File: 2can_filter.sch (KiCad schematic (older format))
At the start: 17 parts

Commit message: finish scheme & change libs path
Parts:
- removed C? (x2): 10pF, symbol C
- removed J?: USB_OTG, symbol USB_OTG
- removed R? (x2): 60, symbol R
- removed R?: 10k, symbol R
- removed U?: STM32F105RBTx, LQFP64, symbol STM32F105RBTx
- removed U?: TJA1040T, Housings_SOIC:SOIC-8_3.9x4.9mm_Pitch1.27mm, symbol TJA1040T
- added C11, C12: 10pF, symbol C
- added J3: USB mini-B SMD, 54819-0572:MOLEXMINIBTYPEB_1, symbol 54819-0572
- added R2: 10k, symbol R
- added R3, R4: 60, symbol R
- added R? (x2): 22, symbol R
- added U5: STM32F105RBTx, Housings_QFP:LQFP-64_10x10mm_Pitch0.5mm, symbol STM32F105RBTx
- added U6: TJA1040T, Housings_SOIC:SOIC-8_3.9x4.9mm_Pitch1.27mm, symbol TJA1040T
- gave numbers to parts that had none: 9
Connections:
- wire segments 75 -> 77
- no-connect marks 43 -> 42
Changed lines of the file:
@@
 LIBS:LM2596SX-5.0_NOPB
 LIBS:lm2575s-5
+LIBS:74HC4050D
+LIBS:54819-0572
 LIBS:instrument_cluster-cache
 EELAYER 25 0
@@
 $EndDescr
 $Comp
-L STM32F105RBTx U?
-U 1 1 5A047502
+L STM32F105RBTx U5
+U 1 1 5A09EB17
 P 4900 2900
-F 0 "U?" H 2200 4825 50  0000 L BNN
+F 0 "U5" H 2200 4825 50  0000 L BNN
 F 1 "STM32F105RBTx" H 7600 4825 50  0000 R BNN
-F 2 "LQFP64" H 7600 4775 50  0001 R TNN
+F 2 "Housings_QFP:LQFP-64_10x10mm_Pitch0.5mm" H 7600 4775 50  0001 R TNN
 F 3 "" H 4900 2900 50  0001 C CNN
 	1    4900 2900
@@
 $EndComp
 $Comp
-L TJA1040T U?
-U 1 1 5A047692
+L TJA1040T U6
+U 1 1 5A09EB18
 P 9800 4150
-F 0 "U?" H 9400 4500 50  0000 L CNN
+F 0 "U6" H 9400 4500 50  0000 L CNN
 F 1 "TJA1040T" H 9850 4500 50  0000 L CNN
 F 2 "Housings_SOIC:SOIC-8_3.9x4.9mm_Pitch1.27mm" H 9800 3650 50  0001 C CIN
@@
 CAN2_L
 $Comp
-L TJA1040T U?
+L TJA1040T U7
 U 1 1 5A0478A4
 P 9800 5550
-F 0 "U?" H 9400 5900 50  0000 L CNN
+F 0 "U7" H 9400 5900 50  0000 L CNN
 F 1 "TJA1040T" H 9850 5900 50  0000 L CNN
 F 2 "Housings_SOIC:SOIC-8_3.9x4.9mm_Pitch1.27mm" H 9800 5050 50  0001 C CIN
@@
 	1500 6500 1950 6500
 $Comp
-L C C?
-U 1 1 5A047AB3
+L C C11
+U 1 1 5A09EB1A
 P 10900 4450
-F 0 "C?" H 10925 4550 50  0000 L CNN
+F 0 "C11" H 10925 4550 50  0000 L CNN
 F 1 "10pF" H 10925 4350 50  0000 L CNN
 F 2 "" H 10938 4300 50  0001 C CNN
@@
 $EndComp
 $Comp
-L R R?
-U 1 1 5A047B18
+L R R4
+U 1 1 5A09EB1B
 P 10650 4250
-F 0 "R?" V 10730 4250 50  0000 C CNN
+F 0 "R4" V 10730 4250 50  0000 C CNN
 F 1 "60" V 10650 4250 50  0000 C CNN
 F 2 "" V 10580 4250 50  0001 C CNN
@@
 $EndComp
 $Comp
-L R R?
-U 1 1 5A047B5E
+L R R3
+U 1 1 5A09EB1C
 P 10650 4050
-F 0 "R?" V 10730 4050 50  0000 C CNN
+F 0 "R3" V 10730 4050 50  0000 C CNN
 F 1 "60" V 10650 4050 50  0000 C CNN
 F 2 "" V 10580 4050 50  0001 C CNN
@@
 +3V3
 $Comp
-L GND #PWR?
-U 1 1 5A047DA1
+L GND #PWR012
+U 1 1 5A09EB1D
 P 1750 6600
-F 0 "#PWR?" H 1750 6350 50  0001 C CNN
+F 0 "#PWR012" H 1750 6350 50  0001 C CNN
 F 1 "GND" H 1750 6450 50  0000 C CNN
 F 2 "" H 1750 6600 50  0001 C CNN
@@
 Connection ~ 4800 5000
 $Comp
-L GND #PWR?
-U 1 1 5A0480FC
+L GND #PWR013
+U 1 1 5A09EB1E
 P 4900 5100
-F 0 "#PWR?" H 4900 4850 50  0001 C CNN
+F 0 "#PWR013" H 4900 4850 50  0001 C CNN
 F 1 "GND" H 4900 4950 50  0000 C CNN
 F 2 "" H 4900 5100 50  0001 C CNN
@@
 Connection ~ 10900 4150
 $Comp
-L C C?
-U 1 1 5A048753
+L C C12
+U 1 1 5A09EB1F
 P 10900 5850
-F 0 "C?" H 10925 5950 50  0000 L CNN
+F 0 "C12" H 10925 5950 50  0000 L CNN
 F 1 "10pF" H 10925 5750 50  0000 L CNN
 F 2 "" H 10938 5700 50  0001 C CNN
@@
 $EndComp
 $Comp
-L R R?
+L R R6
 U 1 1 5A048759
 P 10650 5650
-F 0 "R?" V 10730 5650 50  0000 C CNN
+F 0 "R6" V 10730 5650 50  0000 C CNN
 F 1 "60" V 10650 5650 50  0000 C CNN
 F 2 "" V 10580 5650 50  0001 C CNN
@@
 $EndComp
 $Comp
-L R R?
+L R R5
 U 1 1 5A04875F
 P 10650 5450
-F 0 "R?" V 10730 5450 50  0000 C CNN
+F 0 "R5" V 10730 5450 50  0000 C CNN
 F 1 "60" V 10650 5450 50  0000 C CNN
 F 2 "" V 10580 5450 50  0001 C CNN
@@
 	8800 3950 9300 3950
 $Comp
-L R R?
+L R R1
 U 1 1 5A048BC2
 P 9200 4600
-F 0 "R?" V 9280 4600 50  0000 C CNN
+F 0 "R1" V 9280 4600 50  0000 C CNN
 F 1 "10k" V 9200 4600 50  0000 C CNN
 F 2 "" V 9130 4600 50  0001 C CNN
@@
 	9200 4750 9200 4800
 $Comp
-L GND #PWR?
+L GND #PWR014
 U 1 1 5A048D0B
 P 9800 4650
-F 0 "#PWR?" H 9800 4400 50  0001 C CNN
+F 0 "#PWR014" H 9800 4400 50  0001 C CNN
 F 1 "GND" H 9800 4500 50  0000 C CNN
 F 2 "" H 9800 4650 50  0001 C CNN
@@
 	9800 4550 9800 4650
 $Comp
-L GND #PWR?
-U 1 1 5A048D93
+L GND #PWR015
+U 1 1 5A09EB24
 P 10900 4650
-F 0 "#PWR?" H 10900 4400 50  0001 C CNN
+F 0 "#PWR015" H 10900 4400 50  0001 C CNN
 F 1 "GND" H 10900 4500 50  0000 C CNN
 F 2 "" H 10900 4650 50  0001 C CNN
@@
 	10900 4650 10900 4600
 $Comp
-L GND #PWR?
-U 1 1 5A048E0B
+L GND #PWR016
+U 1 1 5A09EB25
 P 9200 4800
-F 0 "#PWR?" H 9200 4550 50  0001 C CNN
+F 0 "#PWR016" H 9200 4550 50  0001 C CNN
 F 1 "GND" H 9200 4650 50  0000 C CNN
 F 2 "" H 9200 4800 50  0001 C CNN
@@
 $EndComp
 $Comp
-L R R?
-U 1 1 5A048F97
+L R R2
+U 1 1 5A09EB26
 P 9200 6000
-F 0 "R?" V 9280 6000 50  0000 C CNN
+F 0 "R2" V 9280 6000 50  0000 C CNN
 F 1 "10k" V 9200 6000 50  0000 C CNN
 F 2 "" V 9130 6000 50  0001 C CNN
@@
 	9200 6150 9200 6200
 $Comp
-L GND #PWR?
-U 1 1 5A048FA0
+L GND #PWR017
+U 1 1 5A09EB27
 P 9200 6200
-F 0 "#PWR?" H 9200 5950 50  0001 C CNN
+F 0 "#PWR017" H 9200 5950 50  0001 C CNN
 F 1 "GND" H 9200 6050 50  0000 C CNN
 F 2 "" H 9200 6200 50  0001 C CNN
@@
 $EndComp
 $Comp
-L GND #PWR?
-U 1 1 5A049172
+L GND #PWR018
+U 1 1 5A09EB28
 P 9800 6050
-F 0 "#PWR?" H 9800 5800 50  0001 C CNN
+F 0 "#PWR018" H 9800 5800 50  0001 C CNN
 F 1 "GND" H 9800 5900 50  0000 C CNN
 F 2 "" H 9800 6050 50  0001 C CNN
@@
 	9800 5950 9800 6050
 $Comp
-L GND #PWR?
+L GND #PWR019
 U 1 1 5A0491F4
 P 10900 6100
-F 0 "#PWR?" H 10900 5850 50  0001 C CNN
+F 0 "#PWR019" H 10900 5850 50  0001 C CNN
 F 1 "GND" H 10900 5950 50  0000 C CNN
 F 2 "" H 10900 6100 50  0001 C CNN
@@
 	10900 6000 10900 6100
 $Comp
-L D D?
+L D D7
 U 1 1 5A0494E2
 P 2100 6500
-F 0 "D?" H 2100 6400 50  0000 C CNN
+F 0 "D7" H 2100 6400 50  0000 C CNN
 F 1 "PMLL4148L.115" H 2000 6600 50  0000 C CNN
 F 2 "Diodes_SMD:D_SC-80" H 2100 6500 50  0001 C CNN
@@
 $EndComp
 $Comp
-L Conn_01x04_Male J?
+L Conn_01x04_Male J4
 U 1 1 5A0495DE
 P 8950 2700
-F 0 "J?" H 8950 2900 50  0000 C CNN
+F 0 "J4" H 8950 2900 50  0000 C CNN
 F 1 "NOT_FITTED_SWD_Conn_01x04_Male" H 8750 2300 50  0000 C CNN
 F 2 "" H 8950 2700 50  0001 C CNN
@@
 	8750 2950 8750 2800
 $Comp
-L GND #PWR?
+L GND #PWR020
 U 1 1 5A0498E0
 P 8750 2950
-F 0 "#PWR?" H 8750 2700 50  0001 C CNN
+F 0 "#PWR020" H 8750 2700 50  0001 C CNN
 F 1 "GND" H 8750 2800 50  0000 C CNN
 F 2 "" H 8750 2950 50  0001 C CNN
@@
 Connection ~ 2600 6500
 $Comp
-L Crystal Y?
+L Crystal Y1
 U 1 1 5A04A56A
 P 1350 3150
-F 0 "Y?" H 1350 3300 50  0000 C CNN
+F 0 "Y1" H 1350 3300 50  0000 C CNN
 F 1 "Crystal KX-7 25MHz" H 1300 3450 50  0000 C CNN
 F 2 "" H 1350 3150 50  0001 C CNN
@@
 $EndComp
 $Comp
-L C C?
+L C C10
 U 1 1 5A04A61B
 P 1650 3400
-F 0 "C?" H 1675 3500 50  0000 L CNN
+F 0 "C10" H 1675 3500 50  0000 L CNN
 F 1 "12pF" H 1675 3300 50  0000 L CNN
 F 2 "" H 1688 3250 50  0001 C CNN
@@
 $EndComp
 $Comp
-L C C?
+L C C9
 U 1 1 5A04A6A5
 P 1050 3400
-F 0 "C?" H 1075 3500 50  0000 L CNN
+F 0 "C9" H 1075 3500 50  0000 L CNN
 F 1 "12pF" H 1075 3300 50  0000 L CNN
 F 2 "" H 1088 3250 50  0001 C CNN
@@
 $EndComp
 $Comp
-L GND #PWR?
+L GND #PWR021
 U 1 1 5A04A703
 P 1050 3650
-F 0 "#PWR?" H 1050 3400 50  0001 C CNN
+F 0 "#PWR021" H 1050 3400 50  0001 C CNN
 F 1 "GND" H 1050 3500 50  0000 C CNN
 F 2 "" H 1050 3650 50  0001 C CNN
@@
 $EndComp
 $Comp
-L GND #PWR?
+L GND #PWR022
 U 1 1 5A04A747
 P 1650 3650
-F 0 "#PWR?" H 1650 3400 50  0001 C CNN
+F 0 "#PWR022" H 1650 3400 50  0001 C CNN
 F 1 "GND" H 1650 3500 50  0000 C CNN
 F 2 "" H 1650 3650 50  0001 C CNN
@@
 Connection ~ 1650 3150
 $Comp
-L USB_OTG J?
-U 1 1 5A04AFEB
-P 4750 6400
-F 0 "J?" H 4550 6850 50  0000 L CNN
-F 1 "USB_OTG" H 4550 6750 50  0000 L CNN
-F 2 "" H 4900 6350 50  0001 C CNN
-F 3 "" H 4900 6350 50  0001 C CNN
-	1    4750 6400
-	1    0    0    -1
-$EndComp
-$Comp
-L GND #PWR?
+L GND #PWR023
 U 1 1 5A04B0EB
-P 4700 6900
-F 0 "#PWR?" H 4700 6650 50  0001 C CNN
-F 1 "GND" H 4700 6750 50  0000 C CNN
-F 2 "" H 4700 6900 50  0001 C CNN
-F 3 "" H 4700 6900 50  0001 C CNN
-	1    4700 6900
-	1    0    0    -1
-$EndComp
-Wire Wire Line
-	4650 6800 4650 6850
-Wire Wire Line
-	4650 6850 4750 6850
-Wire Wire Line
-	4750 6850 4750 6800
-Wire Wire Line
-	4700 6900 4700 6850
-Connection ~ 4700 6850
-Text Label 5050 6400 0    60   ~ 0
+P 5750 6500
+F 0 "#PWR023" H 5750 6250 50  0001 C CNN
+F 1 "GND" H 5750 6350 50  0000 C CNN
+F 2 "" H 5750 6500 50  0001 C CNN
+F 3 "" H 5750 6500 50  0001 C CNN
+	1    5750 6500
+	1    0    0    -1
+$EndComp
+Text Label 4000 6500 2    60   ~ 0
 USB_D+
-Text Label 5050 6500 0    60   ~ 0
+Text Label 4000 6400 2    60   ~ 0
 USB_D-
-NoConn ~ 5050 6600
-Text Label 5050 6200 0    60   ~ 0
+Text Label 4800 6300 2    60   ~ 0
 USB_Vbus
 Text Label 7700 2400 0    60   ~ 0
@@
 NoConn ~ 2100 1500
 NoConn ~ 2100 1300
+$Comp
+L 54819-0572 J3
+U 1 1 5A09A3F6
+P 4800 6300
+F 0 "J3" H 5150 6450 50  0000 C CNN
+F 1 "USB mini-B SMD" H 5250 5950 50  0000 C CNN
+F 2 "54819-0572:MOLEXMINIBTYPEB_1" H 5150 5850 50  0001 C CNN
+F 3 "http://www.molex.com/webdocs/datasheets/pdf/en-us/0548190572_IO_CONNECTORS.pdf" H 5150 5750 50  0001 C CNN
+F 4 "Surface mount onthego connector,1A 30V Molex On-The-Go Series Right Angle SMT Version 2.0 Type B Mini USB Connector Receptacle, 30 V, 1A" H 5150 5650 50  0001 C CNN "Description"
+F 5 "RS" H 5150 5550 50  0001 C CNN "Supplier_Name"
+F 6 "5151995P" H 5150 5450 50  0001 C CNN "RS Part Number"
+F 7 "Molex" H 5150 5350 50  0001 C CNN "Manufacturer_Name"
+F 8 "54819-0572" H 5150 5250 50  0001 C CNN "Manufacturer_Part_Number"
+F 9 "70266924" H 5150 5150 50  0001 C CNN "Allied_Number"
+	1    4800 6300
+	1    0    0    -1
+$EndComp
+Wire Wire Line
+	5650 6400 5750 6400
+Wire Wire Line
+	5750 6400 5750 6500
+$Comp
+L R R?
+U 1 1 5A0C2815
+P 4550 6400
+F 0 "R?" V 4630 6400 50  0000 C CNN
+F 1 "22" V 4550 6400 50  0000 C CNN
+F 2 "" V 4480 6400 50  0001 C CNN
+F 3 "" H 4550 6400 50  0001 C CNN
+	1    4550 6400
+	0    1    1    0
+$EndComp
+$Comp
+L R R?
+U 1 1 5A0C28CE
+P 4250 6500
+F 0 "R?" V 4330 6500 50  0000 C CNN
+F 1 "22" V 4250 6500 50  0000 C CNN
+F 2 "" V 4180 6500 50  0001 C CNN
+F 3 "" H 4250 6500 50  0001 C CNN
+	1    4250 6500
+	0    1    1    0
+$EndComp
+Wire Wire Line
+	4000 6400 4400 6400
+Wire Wire Line
+	4700 6400 4800 6400
+Wire Wire Line
+	4800 6500 4400 6500
+Wire Wire Line
+	4100 6500 4000 6500
 $EndSCHEMATC

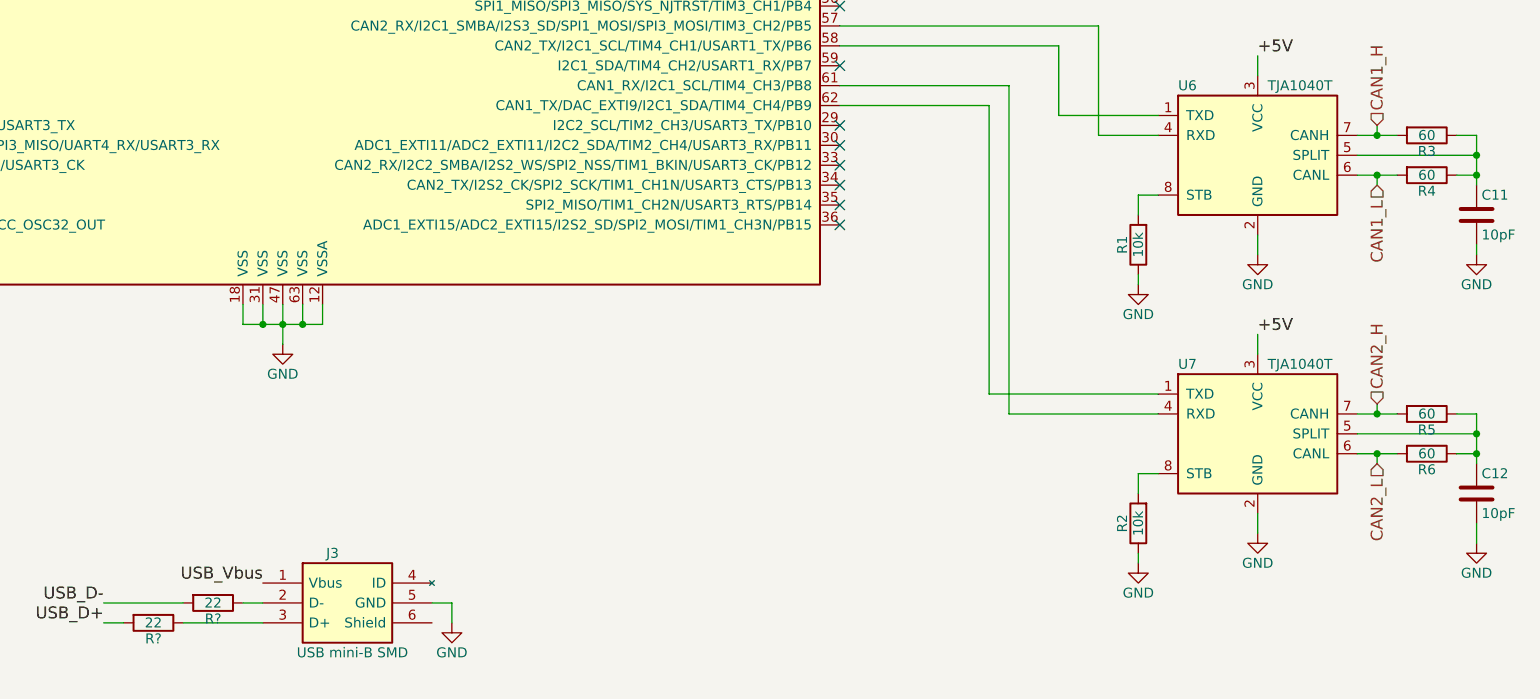
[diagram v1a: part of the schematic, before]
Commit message: specify footpints to resistors and capasitors
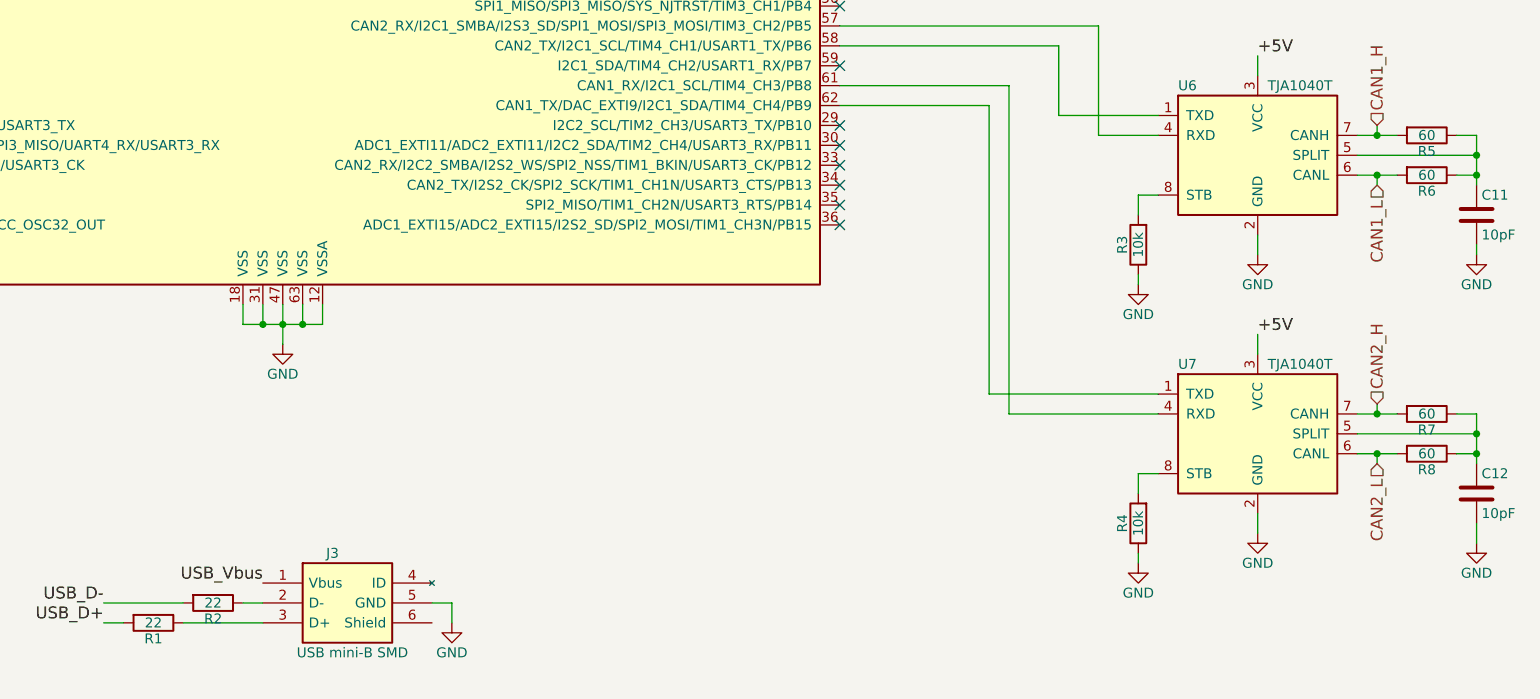
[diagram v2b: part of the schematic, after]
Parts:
- C10, C11, C12, C9: footprint (none) -> Capacitors_SMD:C_0805
- R1, R2: renamed from R?; footprint (none) -> Resistors_SMD:R_0805
- R3: renamed from R1; footprint (none) -> Resistors_SMD:R_0805
- R4: renamed from R2; footprint (none) -> Resistors_SMD:R_0805
- R5: renamed from R3; footprint (none) -> Resistors_SMD:R_0805
- R6: renamed from R4; footprint (none) -> Resistors_SMD:R_0805
- R7: renamed from R5; footprint (none) -> Resistors_SMD:R_0805
- R8: renamed from R6; footprint (none) -> Resistors_SMD:R_0805
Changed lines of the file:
@@
 F 0 "C11" H 10925 4550 50  0000 L CNN
 F 1 "10pF" H 10925 4350 50  0000 L CNN
-F 2 "" H 10938 4300 50  0001 C CNN
+F 2 "Capacitors_SMD:C_0805" H 10938 4300 50  0001 C CNN
 F 3 "" H 10900 4450 50  0001 C CNN
 	1    10900 4450
@@
 $EndComp
 $Comp
-L R R4
+L R R6
 U 1 1 5A09EB1B
 P 10650 4250
-F 0 "R4" V 10730 4250 50  0000 C CNN
+F 0 "R6" V 10730 4250 50  0000 C CNN
 F 1 "60" V 10650 4250 50  0000 C CNN
-F 2 "" V 10580 4250 50  0001 C CNN
+F 2 "Resistors_SMD:R_0805" V 10580 4250 50  0001 C CNN
 F 3 "" H 10650 4250 50  0001 C CNN
 	1    10650 4250
@@
 $EndComp
 $Comp
-L R R3
+L R R5
 U 1 1 5A09EB1C
 P 10650 4050
-F 0 "R3" V 10730 4050 50  0000 C CNN
+F 0 "R5" V 10730 4050 50  0000 C CNN
 F 1 "60" V 10650 4050 50  0000 C CNN
-F 2 "" V 10580 4050 50  0001 C CNN
+F 2 "Resistors_SMD:R_0805" V 10580 4050 50  0001 C CNN
 F 3 "" H 10650 4050 50  0001 C CNN
 	1    10650 4050
@@
 +3V3
 $Comp
-L GND #PWR012
+L GND #PWR14
 U 1 1 5A09EB1D
 P 1750 6600
-F 0 "#PWR012" H 1750 6350 50  0001 C CNN
+F 0 "#PWR14" H 1750 6350 50  0001 C CNN
 F 1 "GND" H 1750 6450 50  0000 C CNN
 F 2 "" H 1750 6600 50  0001 C CNN
@@
 Connection ~ 4800 5000
 $Comp
-L GND #PWR013
+L GND #PWR15
 U 1 1 5A09EB1E
 P 4900 5100
-F 0 "#PWR013" H 4900 4850 50  0001 C CNN
+F 0 "#PWR15" H 4900 4850 50  0001 C CNN
 F 1 "GND" H 4900 4950 50  0000 C CNN
 F 2 "" H 4900 5100 50  0001 C CNN
@@
 F 0 "C12" H 10925 5950 50  0000 L CNN
 F 1 "10pF" H 10925 5750 50  0000 L CNN
-F 2 "" H 10938 5700 50  0001 C CNN
+F 2 "Capacitors_SMD:C_0805" H 10938 5700 50  0001 C CNN
 F 3 "" H 10900 5850 50  0001 C CNN
 	1    10900 5850
@@
 $EndComp
 $Comp
-L R R6
+L R R8
 U 1 1 5A048759
 P 10650 5650
-F 0 "R6" V 10730 5650 50  0000 C CNN
+F 0 "R8" V 10730 5650 50  0000 C CNN
 F 1 "60" V 10650 5650 50  0000 C CNN
-F 2 "" V 10580 5650 50  0001 C CNN
+F 2 "Resistors_SMD:R_0805" V 10580 5650 50  0001 C CNN
 F 3 "" H 10650 5650 50  0001 C CNN
 	1    10650 5650
@@
 $EndComp
 $Comp
-L R R5
+L R R7
 U 1 1 5A04875F
 P 10650 5450
-F 0 "R5" V 10730 5450 50  0000 C CNN
+F 0 "R7" V 10730 5450 50  0000 C CNN
 F 1 "60" V 10650 5450 50  0000 C CNN
-F 2 "" V 10580 5450 50  0001 C CNN
+F 2 "Resistors_SMD:R_0805" V 10580 5450 50  0001 C CNN
 F 3 "" H 10650 5450 50  0001 C CNN
 	1    10650 5450
@@
 	8800 3950 9300 3950
 $Comp
-L R R1
+L R R3
 U 1 1 5A048BC2
 P 9200 4600
-F 0 "R1" V 9280 4600 50  0000 C CNN
+F 0 "R3" V 9280 4600 50  0000 C CNN
 F 1 "10k" V 9200 4600 50  0000 C CNN
-F 2 "" V 9130 4600 50  0001 C CNN
+F 2 "Resistors_SMD:R_0805" V 9130 4600 50  0001 C CNN
 F 3 "" H 9200 4600 50  0001 C CNN
 	1    9200 4600
@@
 	9200 4750 9200 4800
 $Comp
-L GND #PWR014
+L GND #PWR20
 U 1 1 5A048D0B
 P 9800 4650
-F 0 "#PWR014" H 9800 4400 50  0001 C CNN
+F 0 "#PWR20" H 9800 4400 50  0001 C CNN
 F 1 "GND" H 9800 4500 50  0000 C CNN
 F 2 "" H 9800 4650 50  0001 C CNN
@@
 	9800 4550 9800 4650
 $Comp
-L GND #PWR015
+L GND #PWR22
 U 1 1 5A09EB24
 P 10900 4650
-F 0 "#PWR015" H 10900 4400 50  0001 C CNN
+F 0 "#PWR22" H 10900 4400 50  0001 C CNN
 F 1 "GND" H 10900 4500 50  0000 C CNN
 F 2 "" H 10900 4650 50  0001 C CNN
@@
 	10900 4650 10900 4600
 $Comp
-L GND #PWR016
+L GND #PWR18
 U 1 1 5A09EB25
 P 9200 4800
-F 0 "#PWR016" H 9200 4550 50  0001 C CNN
+F 0 "#PWR18" H 9200 4550 50  0001 C CNN
 F 1 "GND" H 9200 4650 50  0000 C CNN
 F 2 "" H 9200 4800 50  0001 C CNN
@@
 $EndComp
 $Comp
-L R R2
+L R R4
 U 1 1 5A09EB26
 P 9200 6000
-F 0 "R2" V 9280 6000 50  0000 C CNN
+F 0 "R4" V 9280 6000 50  0000 C CNN
 F 1 "10k" V 9200 6000 50  0000 C CNN
-F 2 "" V 9130 6000 50  0001 C CNN
+F 2 "Resistors_SMD:R_0805" V 9130 6000 50  0001 C CNN
 F 3 "" H 9200 6000 50  0001 C CNN
 	1    9200 6000
@@
 	9200 6150 9200 6200
 $Comp
-L GND #PWR017
+L GND #PWR19
 U 1 1 5A09EB27
 P 9200 6200
-F 0 "#PWR017" H 9200 5950 50  0001 C CNN
+F 0 "#PWR19" H 9200 5950 50  0001 C CNN
 F 1 "GND" H 9200 6050 50  0000 C CNN
 F 2 "" H 9200 6200 50  0001 C CNN
@@
 $EndComp
 $Comp
-L GND #PWR018
+L GND #PWR21
 U 1 1 5A09EB28
 P 9800 6050
-F 0 "#PWR018" H 9800 5800 50  0001 C CNN
+F 0 "#PWR21" H 9800 5800 50  0001 C CNN
 F 1 "GND" H 9800 5900 50  0000 C CNN
 F 2 "" H 9800 6050 50  0001 C CNN
@@
 	9800 5950 9800 6050
 $Comp
-L GND #PWR019
+L GND #PWR23
 U 1 1 5A0491F4
 P 10900 6100
-F 0 "#PWR019" H 10900 5850 50  0001 C CNN
+F 0 "#PWR23" H 10900 5850 50  0001 C CNN
 F 1 "GND" H 10900 5950 50  0000 C CNN
 F 2 "" H 10900 6100 50  0001 C CNN
@@
 	8750 2950 8750 2800
 $Comp
-L GND #PWR020
+L GND #PWR17
 U 1 1 5A0498E0
 P 8750 2950
-F 0 "#PWR020" H 8750 2700 50  0001 C CNN
+F 0 "#PWR17" H 8750 2700 50  0001 C CNN
 F 1 "GND" H 8750 2800 50  0000 C CNN
 F 2 "" H 8750 2950 50  0001 C CNN
@@
 F 0 "C10" H 1675 3500 50  0000 L CNN
 F 1 "12pF" H 1675 3300 50  0000 L CNN
-F 2 "" H 1688 3250 50  0001 C CNN
+F 2 "Capacitors_SMD:C_0805" H 1688 3250 50  0001 C CNN
 F 3 "" H 1650 3400 50  0001 C CNN
 	1    1650 3400
@@
 F 0 "C9" H 1075 3500 50  0000 L CNN
 F 1 "12pF" H 1075 3300 50  0000 L CNN
-F 2 "" H 1088 3250 50  0001 C CNN
+F 2 "Capacitors_SMD:C_0805" H 1088 3250 50  0001 C CNN
 F 3 "" H 1050 3400 50  0001 C CNN
 	1    1050 3400
@@
 $EndComp
 $Comp
-L GND #PWR021
+L GND #PWR12
 U 1 1 5A04A703
 P 1050 3650
-F 0 "#PWR021" H 1050 3400 50  0001 C CNN
+F 0 "#PWR12" H 1050 3400 50  0001 C CNN
 F 1 "GND" H 1050 3500 50  0000 C CNN
 F 2 "" H 1050 3650 50  0001 C CNN
@@
 $EndComp
 $Comp
-L GND #PWR022
+L GND #PWR13
 U 1 1 5A04A747
 P 1650 3650
-F 0 "#PWR022" H 1650 3400 50  0001 C CNN
+F 0 "#PWR13" H 1650 3400 50  0001 C CNN
 F 1 "GND" H 1650 3500 50  0000 C CNN
 F 2 "" H 1650 3650 50  0001 C CNN
@@
 Connection ~ 1650 3150
 $Comp
-L GND #PWR023
+L GND #PWR16
 U 1 1 5A04B0EB
 P 5750 6500
-F 0 "#PWR023" H 5750 6250 50  0001 C CNN
+F 0 "#PWR16" H 5750 6250 50  0001 C CNN
 F 1 "GND" H 5750 6350 50  0000 C CNN
 F 2 "" H 5750 6500 50  0001 C CNN
@@
 	5750 6400 5750 6500
 $Comp
-L R R?
+L R R2
 U 1 1 5A0C2815
 P 4550 6400
-F 0 "R?" V 4630 6400 50  0000 C CNN
+F 0 "R2" V 4630 6400 50  0000 C CNN
 F 1 "22" V 4550 6400 50  0000 C CNN
-F 2 "" V 4480 6400 50  0001 C CNN
+F 2 "Resistors_SMD:R_0805" V 4480 6400 50  0001 C CNN
 F 3 "" H 4550 6400 50  0001 C CNN
 	1    4550 6400
@@
 $EndComp
 $Comp
-L R R?
+L R R1
 U 1 1 5A0C28CE
 P 4250 6500
-F 0 "R?" V 4330 6500 50  0000 C CNN
+F 0 "R1" V 4330 6500 50  0000 C CNN
 F 1 "22" V 4250 6500 50  0000 C CNN
-F 2 "" V 4180 6500 50  0001 C CNN
+F 2 "Resistors_SMD:R_0805" V 4180 6500 50  0001 C CNN
 F 3 "" H 4250 6500 50  0001 C CNN
 	1    4250 6500
